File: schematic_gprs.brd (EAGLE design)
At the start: 64.9 x 62 mm, 46 parts, among them J1 Jumper Alimentaciones, Q1 MOSFET-NCHANNEL2N7000, Q2 MOSFET-NCHANNEL2N7000, T1 BC547, X1 LTI-SASF54GT

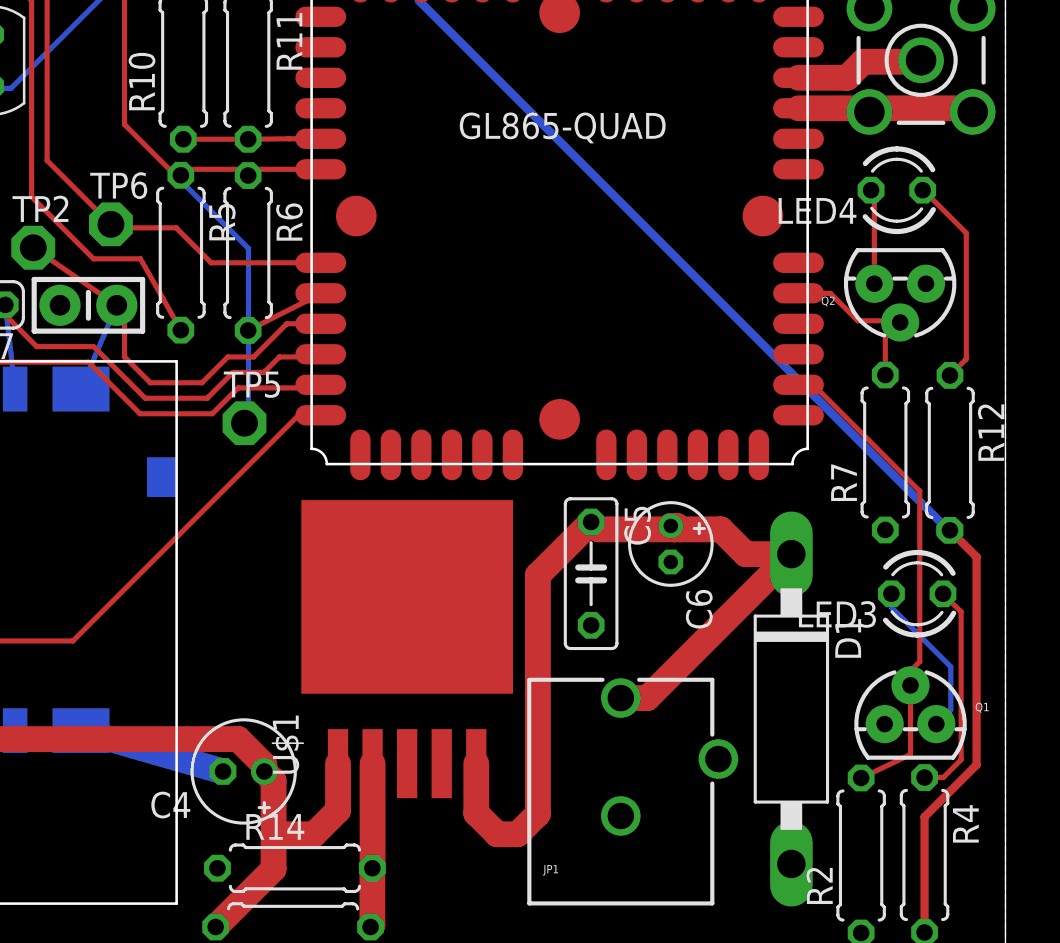
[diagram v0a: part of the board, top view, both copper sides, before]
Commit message: Pistas realizadas
Se acaban todas las conexiones restantes. Se replantean los valores de
las resistencias para el led y se modifican también los valores de las
resistencias a la salida del regulador de tensión. Se añade un
condensador de 1uF a la entrada de VCC de la tarjeta SIM:
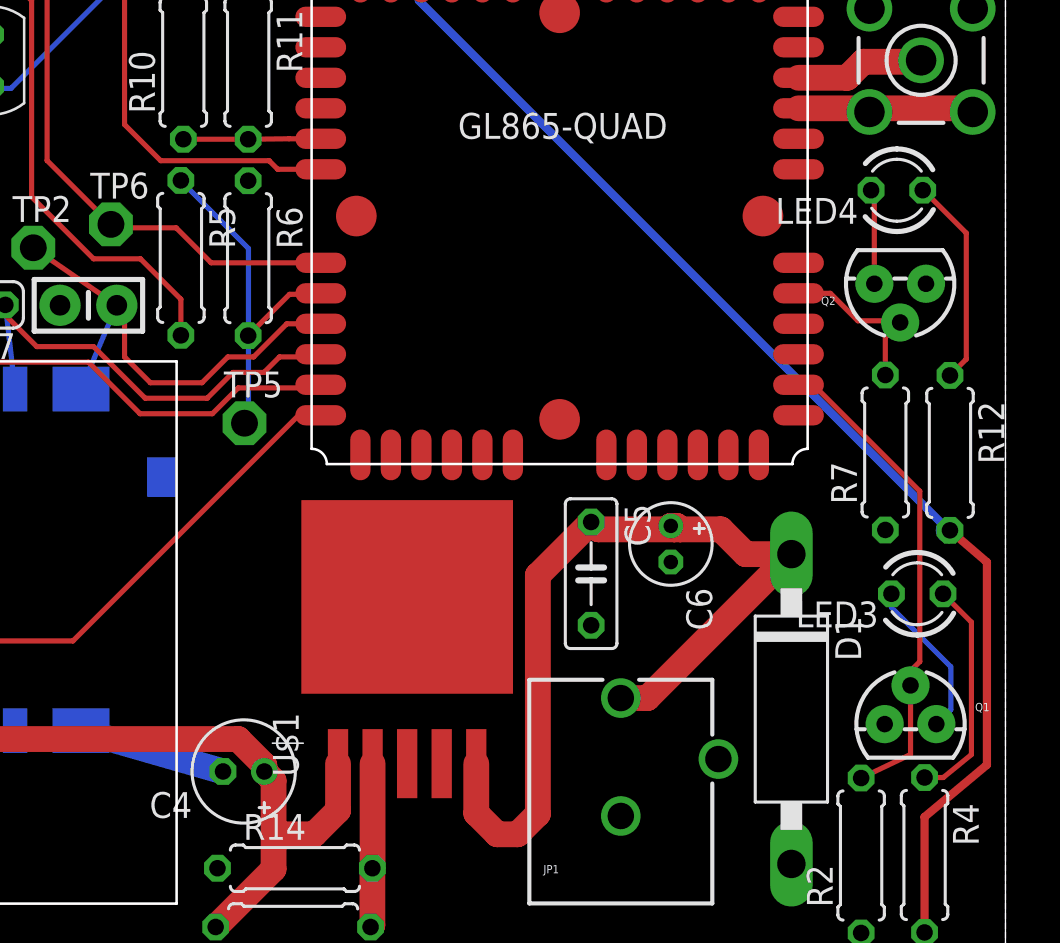
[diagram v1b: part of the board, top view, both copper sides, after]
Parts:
- C4: value (none) -> 10u
- R1: value 180 -> 82
- R13: value 47 -> 68
- moved R5 0.25 mm to (24.4, 35.4)
- moved R6 0.25 mm to (27.7, 35.3)
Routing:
- net VCC: track 122.6 -> 123.3 mm
- net 3.3V_RX: track 34.6 -> 35.1 mm
- net N$12: track 10.7 -> 11.2 mm
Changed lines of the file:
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@@
 </class>
 </classes>
-<designrules name="default">
+<designrules name="default *">
 <description language="de">&lt;b&gt;EAGLE Design Rules&lt;/b&gt;
 &lt;p&gt;
@@
 design rules under a new name.</description>
 <param name="layerSetup" value="(1*16)"/>
-<param name="mtCopper" value="0.035mm 0.035mm 0.035mm 0.035mm 0.035mm 0.035mm 0.035mm 0.035mm 0.035mm 0.035mm 0.035mm 0.035mm 0.035mm 0.035mm 0.035mm 0.035mm"/>
+<param name="mtCopper" value="0.15mm 0.15mm 0.035mm 0.035mm 0.035mm 0.035mm 0.035mm 0.035mm 0.035mm 0.035mm 0.035mm 0.035mm 0.035mm 0.035mm 0.035mm 0.15mm"/>
 <param name="mtIsolate" value="1.5mm 0.15mm 0.2mm 0.15mm 0.2mm 0.15mm 0.2mm 0.15mm 0.2mm 0.15mm 0.2mm 0.15mm 0.2mm 0.15mm 0.2mm"/>
 <param name="mdWireWire" value="8mil"/>
@@
 <element name="R7" library="resistor" package="0207/7" value="100k" x="59.01" y="25.78" rot="R90"/>
 <element name="R8" library="resistor" package="0207/7" value="1k" x="10.934" y="47.392" rot="R90"/>
-<element name="R6" library="resistor" package="0207/7" value="15k" x="27.67" y="35.592" rot="R270"/>
+<element name="R6" library="resistor" package="0207/7" value="15k" x="27.67" y="35.338" rot="R270"/>
 <element name="R10" library="resistor" package="0207/7" value="2.7k" x="24.48" y="44.998" rot="R90"/>
-<element name="R5" library="resistor" package="0207/7" value="2.7k" x="24.36" y="35.606" rot="R270"/>
+<element name="R5" library="resistor" package="0207/7" value="2.7k" x="24.36" y="35.352" rot="R270"/>
 <element name="R11" library="resistor" package="0207/7" value="15k" x="27.67" y="44.998" rot="R270"/>
-<element name="R1" library="resistor" package="0207/7" value="180" x="22.26" y="53.65"/>
+<element name="R1" library="resistor" package="0207/7" value="82" x="22.26" y="53.65"/>
 <element name="R2" library="resistor" package="0207/7" value="100k" x="57.82" y="5.956" rot="R90"/>
 <element name="R4" library="resistor" package="0207/7" value="180" x="60.94" y="5.982" rot="R270"/>
@@
 <element name="J1" library="jumper" package="04C" value="Jumper Alimentaciones" x="4.53" y="51.43" rot="R270"/>
 <element name="L_FERRITE_BEAD1" library="sym" package="0207/7" value="" x="38.31" y="57.08" rot="R90"/>
-<element name="R13" library="resistor" package="0207/7" value="47" x="29.88" y="2.44" rot="R180"/>
-<element name="C4" library="resistor" package="E2-5" value="" x="27.45" y="10.09" rot="R180"/>
+<element name="R13" library="resistor" package="0207/7" value="68" x="29.88" y="2.44" rot="R180"/>
+<element name="C4" library="resistor" package="E2-5" value="10u" x="27.45" y="10.09" rot="R180"/>
 <element name="R14" library="resistor" package="0207/7" value="390" x="29.97" y="5.33"/>
 <element name="C5" library="resistor" package="C050-025X075" value="19n" x="44.54" y="19.82" rot="R270"/>
@@
 <contactref element="R6" pad="2"/>
 <contactref element="TP5" pad="TP"/>
-<wire x1="27.67" y1="31.782" x2="31.19" y2="33.56" width="0.254" layer="1"/>
 <wire x1="31.19" y1="33.56" x2="31.24" y2="33.61" width="0.254" layer="1"/>
 <wire x1="24.36" y1="39.14" x2="27.686" y2="35.814" width="0.254" layer="16"/>
 <wire x1="27.686" y1="35.814" x2="27.686" y2="31.798" width="0.254" layer="16"/>
-<wire x1="27.686" y1="31.798" x2="27.67" y2="31.782" width="0.254" layer="16"/>
-<wire x1="24.36" y1="39.14" x2="24.36" y2="39.416" width="0.254" layer="16"/>
+<wire x1="27.686" y1="31.798" x2="27.67" y2="31.528" width="0.254" layer="16"/>
+<wire x1="24.36" y1="39.14" x2="24.36" y2="39.162" width="0.254" layer="16"/>
 <wire x1="27.686" y1="31.798" x2="27.686" y2="27.416" width="0.254" layer="16"/>
 <wire x1="27.686" y1="27.416" x2="27.49" y2="27.22" width="0.254" layer="16"/>
+<wire x1="31.19" y1="33.56" x2="29.702" y2="33.56" width="0.254" layer="1"/>
+<wire x1="29.702" y1="33.56" x2="27.67" y2="31.528" width="0.254" layer="1"/>
 </signal>
 <signal name="TX_MODULE2ZYBO">
@@
 <contactref element="GSM/GPRS1" pad="C106/CTS"/>
 <contactref element="SV1" pad="P7"/>
-<wire x1="31.24" y1="39.71" x2="23.79" y2="39.71" width="0.254" layer="1"/>
-<wire x1="23.79" y1="39.71" x2="21.59" y2="41.91" width="0.254" layer="1"/>
 <wire x1="21.59" y1="41.91" x2="21.59" y2="50.8" width="0.254" layer="1"/>
 <wire x1="21.59" y1="50.8" x2="20.32" y2="52.07" width="0.254" layer="1"/>
@@
 <wire x1="16.002" y1="57.912" x2="17.27" y2="59.18" width="0.254" layer="1"/>
 <wire x1="17.27" y1="59.18" x2="17.32" y2="59.18" width="0.254" layer="1"/>
+<wire x1="21.59" y1="41.91" x2="23.368" y2="40.132" width="0.254" layer="1"/>
+<wire x1="23.368" y1="40.132" x2="28.702" y2="40.132" width="0.254" layer="1"/>
+<wire x1="28.702" y1="40.132" x2="29.124" y2="39.71" width="0.254" layer="1"/>
+<wire x1="29.124" y1="39.71" x2="31.24" y2="39.71" width="0.254" layer="1"/>
 </signal>
 <signal name="RTS_ZYBO2MODULE">
@@
 <contactref element="R5" pad="2"/>
 <contactref element="SV1" pad="P9"/>
-<wire x1="24.36" y1="31.796" x2="22.374" y2="35.306" width="0.254" layer="1"/>
 <wire x1="22.374" y1="35.306" x2="20.066" y2="35.306" width="0.254" layer="1"/>
 <wire x1="20.066" y1="35.306" x2="17.018" y2="38.354" width="0.254" layer="1"/>
@@
 <wire x1="10.922" y1="57.912" x2="12.19" y2="59.18" width="0.254" layer="1"/>
 <wire x1="12.19" y1="59.18" x2="12.24" y2="59.18" width="0.254" layer="1"/>
+<wire x1="22.374" y1="35.306" x2="24.36" y2="33.32" width="0.254" layer="1"/>
+<wire x1="24.36" y1="33.32" x2="24.36" y2="31.542" width="0.254" layer="1"/>
 </signal>
 <signal name="3.3V_RTS">
@@
 <contactref element="R4" pad="1"/>
 <wire x1="60.94" y1="9.792" x2="61.862" y2="9.792" width="0.254" layer="1"/>
-<wire x1="61.862" y1="9.792" x2="62.738" y2="10.668" width="0.254" layer="1"/>
-<wire x1="62.738" y1="10.668" x2="62.738" y2="17.942" width="0.254" layer="1"/>
-<wire x1="62.738" y1="17.942" x2="61.85" y2="18.83" width="0.254" layer="1"/>
+<wire x1="61.862" y1="9.792" x2="63.246" y2="10.922" width="0.254" layer="1"/>
+<wire x1="63.246" y1="10.922" x2="63.246" y2="17.434" width="0.254" layer="1"/>
+<wire x1="63.246" y1="17.434" x2="61.85" y2="18.83" width="0.254" layer="1"/>
 </signal>
 <signal name="N$9">
@@
 <wire x1="36.068" y1="53.672" x2="36.04" y2="53.7" width="1.27" layer="16"/>
 <wire x1="60.94" y1="2.172" x2="60.94" y2="7.854" width="0.4064" layer="1"/>
-<wire x1="60.94" y1="7.854" x2="63.5" y2="10.414" width="0.4064" layer="1"/>
-<wire x1="63.5" y1="10.414" x2="63.5" y2="20.64" width="0.4064" layer="1"/>
-<wire x1="63.5" y1="20.64" x2="62.19" y2="21.95" width="0.4064" layer="1"/>
+<wire x1="60.94" y1="7.854" x2="64.008" y2="10.414" width="0.4064" layer="1"/>
+<wire x1="64.008" y1="10.414" x2="64.008" y2="20.386" width="0.4064" layer="1"/>
+<wire x1="64.008" y1="20.386" x2="62.19" y2="21.95" width="0.4064" layer="1"/>
 </signal>
 <signal name="N$14">

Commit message: Resultado Final
PCB  a espera de revisión por tutor el día 18/02/2015
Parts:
- moved X1 1.04 mm to (61.8, 45.2)
- moved R9 1.00 mm to (8.70, 47.4)
- moved C1 1.00 mm to (62.5, 54.5)
- moved C10 1.00 mm to (20.8, 33.0)
- moved C2 1.00 mm to (55.6, 55.8)
- moved C3 1.00 mm to (46.7, 55.8)
- moved C4 1.00 mm to (28.4, 10.1)
- moved C5 1.00 mm to (45.5, 19.8)
- moved C6 1.00 mm to (49.5, 21.3)
- moved C7 1.00 mm to (15.5, 33.0)
- moved C8 1.00 mm to (10.6, 33.0)
- moved C9 1.00 mm to (4.29, 16.0)
- moved D1 1.00 mm to (55.4, 13.2)
- moved GSM/GPRS1 1.00 mm to (31.8, 25.2)
- moved J1 1.00 mm to (5.53, 51.4)
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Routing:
- net GND: track 15.9 -> 7.37 mm
- net N$17: track 0.00 -> 1.50 mm
- net N$11: track 44.4 -> 43.7 mm
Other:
- board size 64.9 x 62 mm -> 66.5 x 62.8 mm
